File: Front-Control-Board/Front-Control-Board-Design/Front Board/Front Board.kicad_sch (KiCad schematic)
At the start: 26 parts, among them J1 Conn_01x08, J2 Conn_01x23, Q1 2N7002, U1 MAX33054EASA+T, U2 TS2940CP33 ROG, U3 ESP32-DevKitC

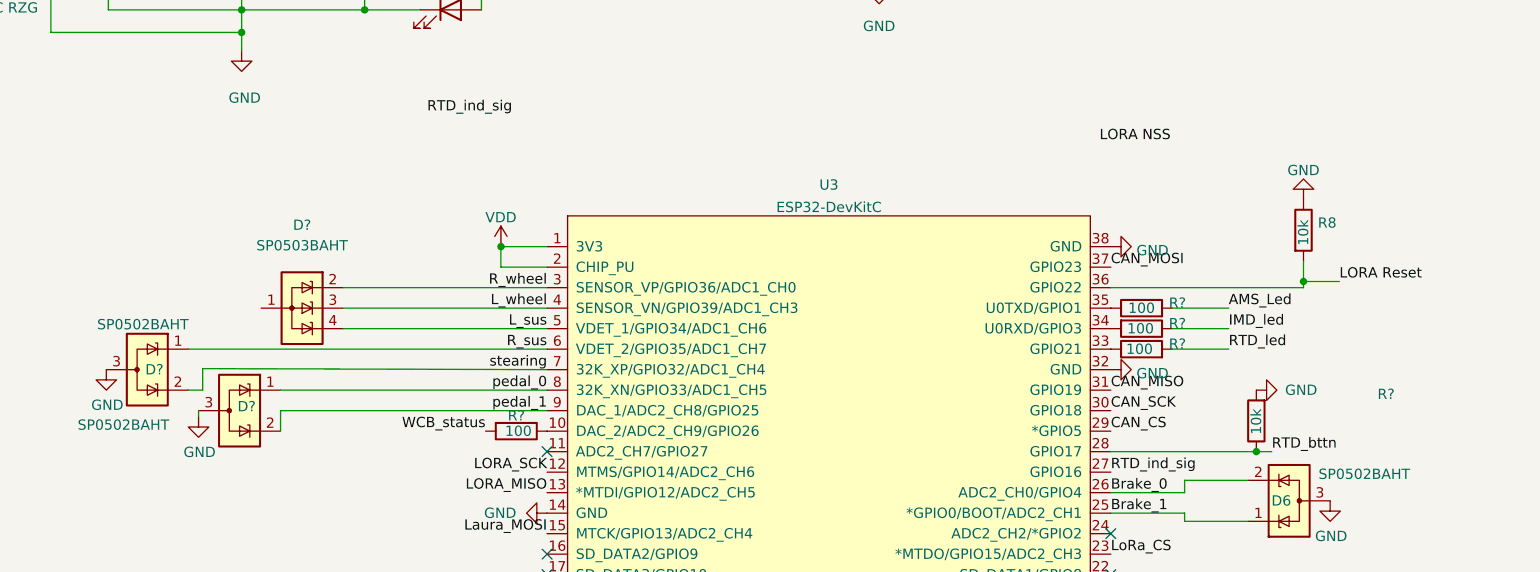
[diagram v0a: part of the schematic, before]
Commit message: pin layout updated needs PCB
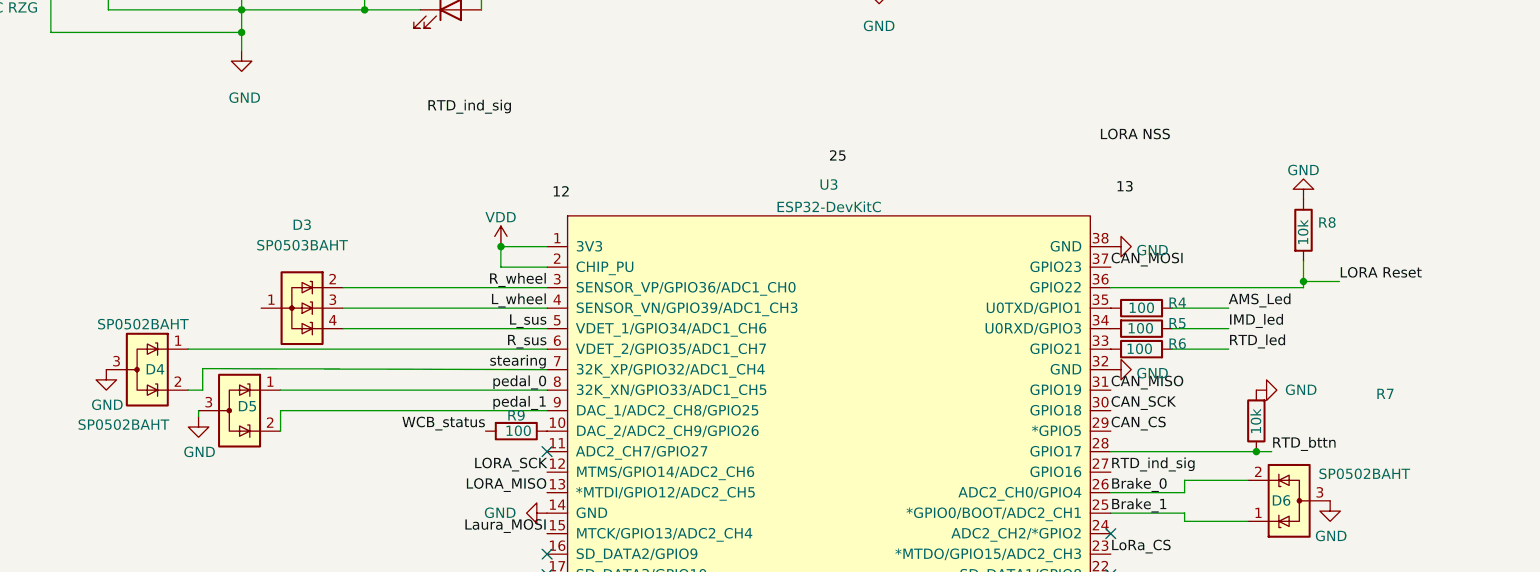
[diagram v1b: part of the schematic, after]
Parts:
- U3: footprint Espressif:ESP32-DevKitC -> AERO_Footprints:ESP32-DEV C
- gave numbers to parts that had none: 8

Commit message: Front board updated just needs traces
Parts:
- U3: footprint AERO_Footprints:ESP32-DEV C -> esp32:ESP32-DevKitC
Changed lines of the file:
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@@
     (property "Reference" "U3" (id 0) (at 122.555 67.9155 0))
     (property "Value" "ESP32-DevKitC" (id 1) (at 122.555 70.6906 0))
-    (property "Footprint" "AERO_Footprints:ESP32-DEV C" (id 2) (at 120.65 128.905 0)
+    (property "Footprint" "esp32:ESP32-DevKitC" (id 2) (at 120.65 128.905 0)
       (effects (font (size 1.27 1.27)) hide)
     )
@@
     )
     (path "/12a6a643-8d09-4828-9fdd-0e9da0628c48"
-      (reference "U3") (unit 1) (value "ESP32-DevKitC") (footprint "AERO_Footprints:ESP32-DEV C")
-    )
-  )
+      (reference "U3") (unit 1) (value "ESP32-DevKitC") (footprint "esp32:ESP32-DevKitC")
+    )
+  )

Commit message: Front Board V1
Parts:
- removed J1: Conn_01x08, AERO_Footprints:TE_1-776280-1_8pin_Horizontal, symbol Connector_Generic:Conn_01x08
- removed J2: Conn_01x23, AERO_Footprints:TE_1-770669-1_23pin_Horizontal, symbol Connector_Generic:Conn_01x23
- added J1, J2: Conn_01x14, AERO_Footprints:TE_1-776266-1_14pin_Horizontal, symbol Connector_Generic:Conn_01x14
- added J3: Conn_01x08, AERO_Footprints:TE_1-776280-1_8pin_Horizontal, symbol Connector_Generic:Conn_01x08
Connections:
- net +12V: now also J1.10 (Pin_10), J3.1 (Pin_1), J3.2 (Pin_2)
- net AMS_Led: now also J2.5 (Pin_5)
- net Brake_0: now also J2.2 (Pin_2)
- net Brake_1: now also J2.6 (Pin_6)
- net CAN_CS: now also U1.8 (STBY)
- net CAN_N: now also D1.2 (K), J2.14 (Pin_14); no longer D1.1 (K)
- net CAN_P: now also D1.1 (K), J2.13 (Pin_13); no longer D1.2 (K)
- net GND: now also D3.1 (A), J1.13 (Pin_13); no longer U1.8 (STBY)
- net IMD_led: now also J2.8 (Pin_8)
- net LORA Reset: now also J2.9 (Pin_9)
- net LORA_MISO: now also J1.5 (Pin_5)
- net LORA_SCK: now also J1.9 (Pin_9)
- net L_sus: now also D3.2 (K), J1.2 (Pin_2); no longer D3.4 (K)
- net L_wheel: now also J1.11 (Pin_11)
- net Laura_MOSI: now also J1.14 (Pin_14)
- net LoRa_CS: now also J2.1 (Pin_1)
- net RTD_bttn: now also J2.7 (Pin_7)
- net RTD_ind_out: now also J2.11 (Pin_11)
- net RTD_led: now also J2.4 (Pin_4)
- net R_sus: now also J1.7 (Pin_7)
- net R_wheel: now also D3.4 (K), J1.1 (Pin_1); no longer D3.2 (K)
- net VDD: now also J1.6 (Pin_6), J3.3 (Pin_3), J3.4 (Pin_4), J3.5 (Pin_5), J3.6 (Pin_6), J3.7 (Pin_7), J3.8 (Pin_8)
- net WCB_status: now also J1.4 (Pin_4)
- net pedal_0: now also J1.12 (Pin_12)
- net pedal_1: now also J1.8 (Pin_8)
- net stearing: now also J1.3 (Pin_3)
- no-connect marks 9 -> 12

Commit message: updates
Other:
- note added: "C.Grund 22.311"
- note added: "FRONT BOARD"
- note added: "Front board -Sensor input, pedals/wheel speed/suspention/wheel position -Wireless communication, Wheel board/LoRa -RTD back up / Indicator -fault lights"
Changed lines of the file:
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@@
     (effects (font (size 2.0066 2.0066)) (justify left bottom))
+  )
+  (text "FRONT BOARD" (at 186.436 190.627 0)
+    (effects (font (size 1.27 1.27)) (justify left bottom))
+  )
+  (text "C.Grund 22.311" (at 187.706 184.277 0)
+    (effects (font (size 1.27 1.27)) (justify left bottom))
+  )
+  (text "Front board \n-Sensor input, pedals/wheel speed/suspention/wheel position\n-Wireless communication, Wheel board/LoRa\n-RTD back up / Indicator\n-fault lights\n"
+    (at 177.8 176.657 0)
+    (effects (font (size 1.27 1.27)) (justify left bottom))
   )
   (text "STBY logic low is normal mode\nlogic high is receive only"
